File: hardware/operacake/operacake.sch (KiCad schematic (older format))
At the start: 129 parts, among them J1 CONN_02X20, J2 CONN_02X20, P1 ADDRESS, P20 GPIO, P22 I2S, P28 SD, P9 BASEBAND, U1 MASWSS0129, U10 74LVC1G58, U11 74LVC1G58, U12 74LVC1G58, U13 74LVC1G58, U14 74AHC1G02, U15 74AHC1G02, U16 74LVC1G19, U2 SKY13322, U3 SKY13322, U4 PCA9557, U5 TC7MBL3245CFT, U6 74LVC1G58, U7 74LVC1G58, U8 74AHC1G08, U9 74AHC1G08

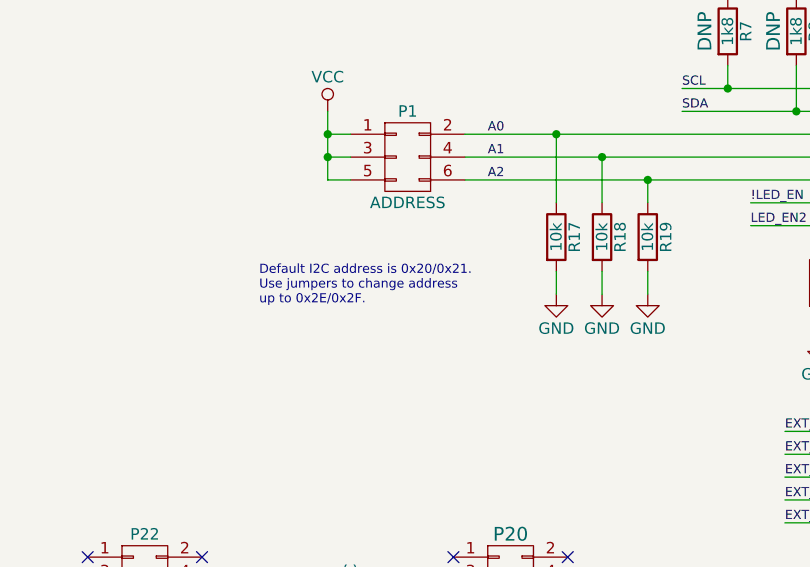
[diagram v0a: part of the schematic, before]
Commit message: Opera Cake: corrected I2C address note in schematic
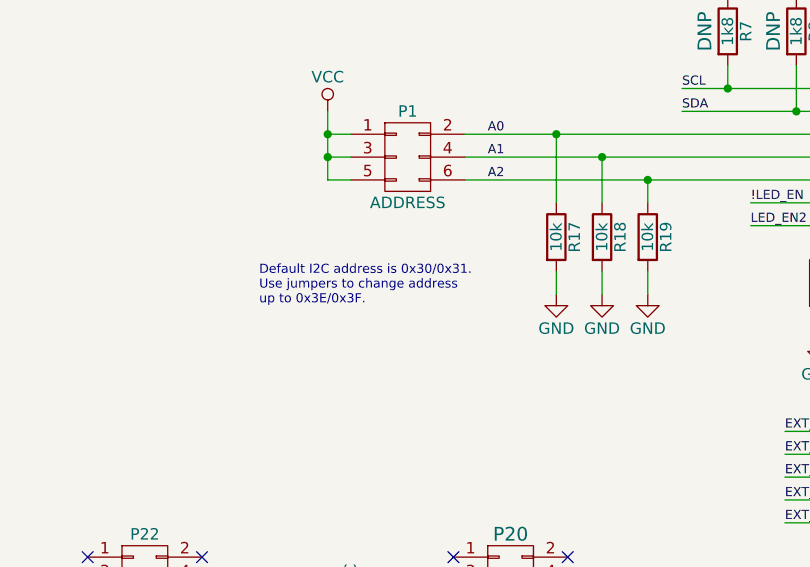
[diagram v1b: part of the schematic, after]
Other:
- note added: "Default I2C address is 0x30/0x31.\nUse jumpers to change address\nup to 0x3E/0x3F."
- note removed: "Default I2C address is 0x20/0x21.\nUse jumpers to change address\nup to 0x2E/0x2F."
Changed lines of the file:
@@
 $EndComp
 Text Notes 7200 7900 0    40   ~ 0
-Default I2C address is 0x20/0x21.\nUse jumpers to change address\nup to 0x2E/0x2F.
+Default I2C address is 0x30/0x31.\nUse jumpers to change address\nup to 0x3E/0x3F.
 Text Label 9350 7550 0    40   ~ 0
 LED_EN2
